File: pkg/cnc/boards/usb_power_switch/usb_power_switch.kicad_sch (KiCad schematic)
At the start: 5 parts, among them J1 USB_A_FEMALE, J2 USB_A_MALE, J3 EN, Q1 DMG2301L

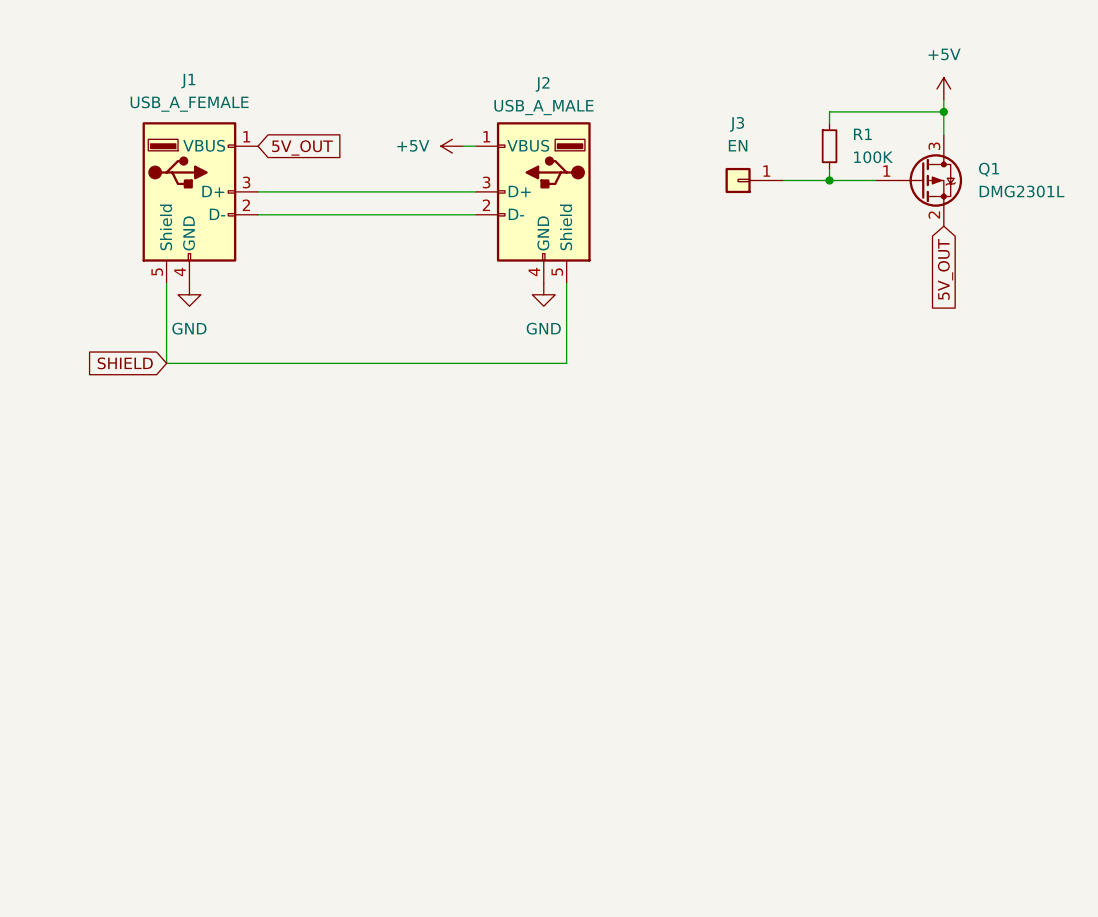
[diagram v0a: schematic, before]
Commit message: Add PCB CAM and Voron toolboard stuff.
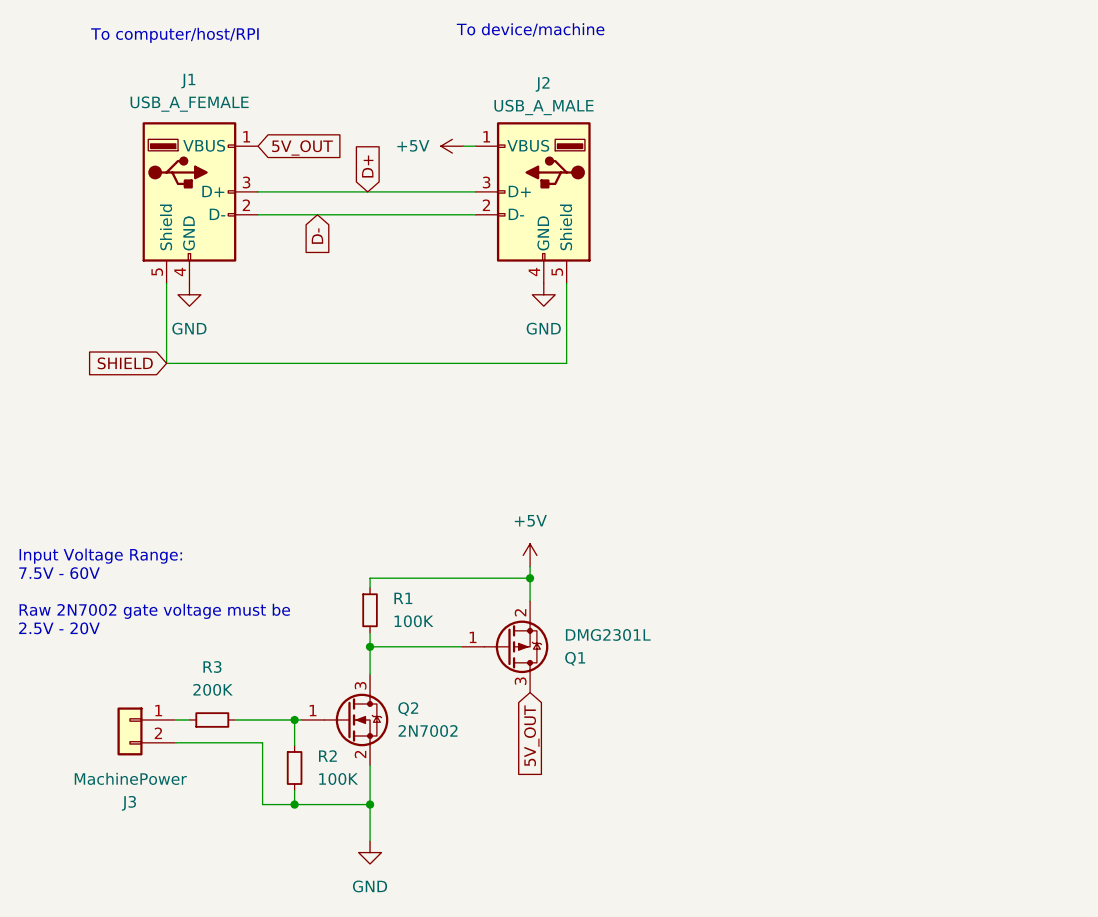
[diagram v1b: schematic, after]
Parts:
- removed J3: EN, Connector_PinHeader_2.54mm:PinHeader_1x01_P2.54mm_Horizontal, symbol Connector_Generic:Conn_01x01
- added J3: MachinePower, Connector_JST:JST_XH_B2B-XH-A_1x02_P2.50mm_Vertical, symbol Connector_Generic:Conn_01x02
- added Q2: 2N7002, Package_TO_SOT_SMD:SOT-23, symbol Transistor_FET:2N7002
- added R2: 100K, Resistor_SMD:R_0603_1608Metric_Pad0.98x0.95mm_HandSolder, symbol Device:R_Small
- added R3: 200K, Resistor_SMD:R_0603_1608Metric_Pad0.98x0.95mm_HandSolder, symbol Device:R_Small
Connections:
- net +5V: now also Q1.2 (S); no longer Q1.3 (D)
- net 5V_OUT: now also Q1.3 (D); no longer Q1.2 (S)
- net GND: now also J3.2 (Pin_2), Q2.2 (S), R2.2
- net at Q1.1 (G), R1.2: now also Q2.3 (D)
- net D-: now reaches J1.2 (D-), J2.2 (D-)
- net D+: now reaches J1.3 (D+), J2.3 (D+)
- new net: J3.1 (Pin_1), R3.1
- new net: Q2.1 (G), R2.1, R3.2
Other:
- note added: "Input Voltage Range: 7.5V - 60V Raw 2N7002 gate voltage must be 2.5V - 20V"
- note added: "To computer/host/RPI"
- note added: "To device/machine"
- moved on the sheet: Q1, R1
